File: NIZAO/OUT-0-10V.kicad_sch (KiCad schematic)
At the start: 5 parts, among them U15 GP8211S-TC50-EW

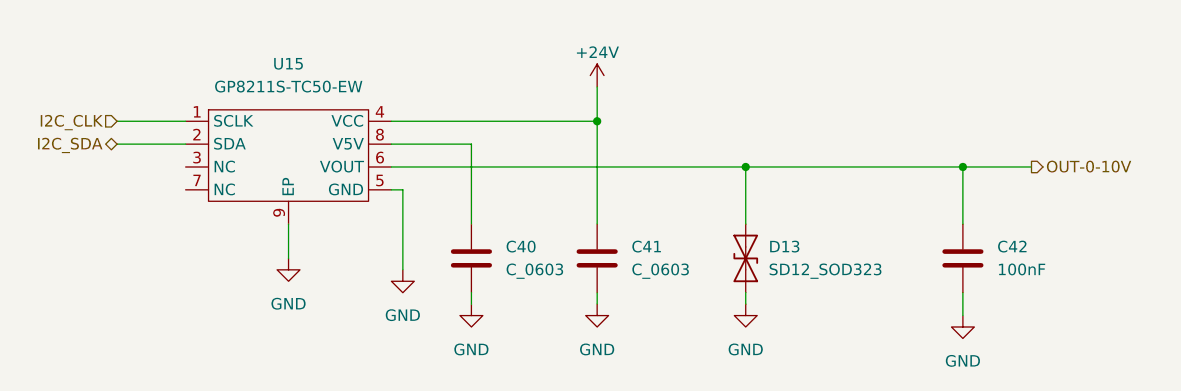
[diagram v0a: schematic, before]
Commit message: Colocandos los 3d de los componetes en la placa NIZAO
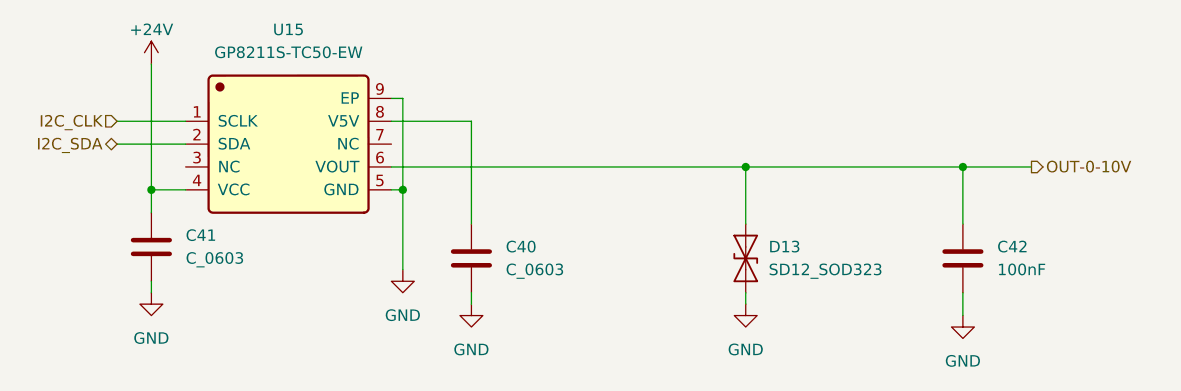
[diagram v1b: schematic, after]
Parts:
- U15: footprint Guestgood GP8211S-TC50-EW:ESOP-8_L4.9-W3.9-P1.27-LS6.0-BL-EP -> JLCImport:GP8211S-TC50-EW; symbol EasyEDA:GP8211S-TC50-EW -> JLCImport:GP8211S-TC50-EW; LCSC (none) -> C3152008; Manufacturer (none) -> Guestgood; Manufacturer Part (none) -> GP8211S-TC50-EW
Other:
- moved on the sheet: C41
